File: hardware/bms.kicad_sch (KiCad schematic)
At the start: 15 parts

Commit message: train schematics
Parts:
- C? (x4): Voltage 10V -> 25V
- C?: value 22u -> 10u; Voltage 10V -> 25V
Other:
- note added: "0x40-0x4E/0x41-0x4F"
- note added: "0x6C/0x6D"
- company: Erdapfel -> Frisius
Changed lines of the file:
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@@
   (title_block
     (rev "A")
-    (company "Erdapfel")
+    (company "Frisius")
   )
   (junction (at 86.36 68.58) (diameter 0) (color 0 0 0 0)
@@
   (wire (pts (xy 46.99 66.04) (xy 46.99 67.31))
     (stroke (width 0) (type default) (color 0 0 0 0))
+  )
+  (text "0x40-0x4E/0x41-0x4F" (at 120.65 27.94 0)
+    (effects (font (size 1.27 1.27)) (justify left bottom))
+  )
+  (text "0x6C/0x6D" (at 120.65 59.69 0)
+    (effects (font (size 1.27 1.27)) (justify left bottom))
   )
   (label "USB_CHG.DP" (at 52.07 35.56 180)
@@
       (effects (font (size 0.8 0.8)) hide)
     )
-    (property "Voltage" "10V" (id 4) (at 88.9 74.93 0)
+    (property "Voltage" "25V" (id 4) (at 88.9 74.93 0)
       (effects (font (size 0.8 0.8)) (justify left))
     )
@@
       (effects (font (size 0.8 0.8)) hide)
     )
-    (property "Voltage" "10V" (id 4) (at 96.52 40.64 0)
+    (property "Voltage" "25V" (id 4) (at 96.52 40.64 0)
       (effects (font (size 0.8 0.8)) (justify left))
     )
@@
       (effects (font (size 0.8 0.8)) hide)
     )
-    (property "Voltage" "10V" (id 4) (at 96.52 58.42 0)
+    (property "Voltage" "25V" (id 4) (at 96.52 58.42 0)
       (effects (font (size 0.8 0.8)) (justify left))
     )
@@
       (effects (font (size 0.8 0.8)) (justify left))
     )
-    (property "Value" "22u" (id 1) (at 104.14 39.37 0)
+    (property "Value" "10u" (id 1) (at 104.14 39.37 0)
       (effects (font (size 0.8 0.8)) (justify left))
     )
@@
       (effects (font (size 0.8 0.8)) hide)
     )
-    (property "Voltage" "10V" (id 4) (at 104.14 40.64 0)
+    (property "Voltage" "25V" (id 4) (at 104.14 40.64 0)
       (effects (font (size 0.8 0.8)) (justify left))
     )
@@
       (effects (font (size 0.8 0.8)) hide)
     )
-    (property "Voltage" "10V" (id 4) (at 104.14 58.42 0)
-      (effects (font (size 0.8 0.8)) (justify left))
-    )
+    (property "Voltage" "25V" (id 4) (at 104.14 58.42 0)
+      (effects (font (size 0.8 0.8)) (justify left))
+    )

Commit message: usb, charger, sensors, heir
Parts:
- added C? (x2): 4.7u, Capacitor_SMD:C_0805_2012Metric, symbol Device:C_Small
- added D? (x2): LED_Small_Filled, symbol Device:LED_Small_Filled
- added R? (x2): 100k, Resistor_SMD:R_0603_1608Metric, symbol Device:R_Small
- added R? (x2): 1k, Resistor_SMD:R_0603_1608Metric, symbol Device:R_Small
- added R? (x3): 0, Resistor_SMD:R_0603_1608Metric, symbol Device:R_Small
- added R?: 100, Resistor_SMD:R_0603_1608Metric, symbol Device:R_Small
- added R? (x2): 14k, Resistor_SMD:R_0603_1608Metric, symbol Device:R_Small
- added R? (x2): 4.7k, Resistor_SMD:R_0603_1608Metric, symbol Device:R_Small
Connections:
- net GND: now also C?.2, C?.2, R?.2, R?.2
- net SENSOR_I2C.SCL: now also R?.2
- net SENSOR_I2C.SDA: now also R?.2
- net USB_SW: now also R?.2
- net +BATT: now reaches BT?.1 (+), C?.1, C?.1, U?.13_14 (BAT), U?.2 (CELL), U?.3 (VDD)
- net +BATT: now also C?.1, R?.2
- net at U?.11 (ITOPOFF): now also R?.1, R?.2
- net at U?.12 (IFAST): now also R?.1
- net at U?.2 (INOKB): now also R?.1, R?.1, R?.2
- net VBUS: now reaches U?.23_24 (CHGIN)
- net VBUS: now also C?.1, C?.1
- net at U?.3 (STAT): now also R?.1, R?.1, R?.2
- net at U?.8 (VCC): now also R?.1; no longer C?.1
- net THERM_SHDN renamed CHG_SHDN
- net CHG_SHDN: now also R?.1
- new net: D?.1 (K), R?.1 (x2)
- new net 3V3_CORE: D?.2 (A), D?.2 (A), R?.1, R?.1, R?.2, R?.2
- new net CHG_STAT: R?.2
- no-connect marks 0 -> 1
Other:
- note added: "DEBUG LEDS"
- note added: "Defaults: T_{th}=80C T_{hys}=75C OS Comparator OS Active Low"
- note added: "Hi-Z till LM75B thermal threshold which triggers thermal shutdown"
- note added: "I_{Fast}=2000mA I_{Topoff}=150mA"
- moved on the sheet: BT?, C?, L?, U?

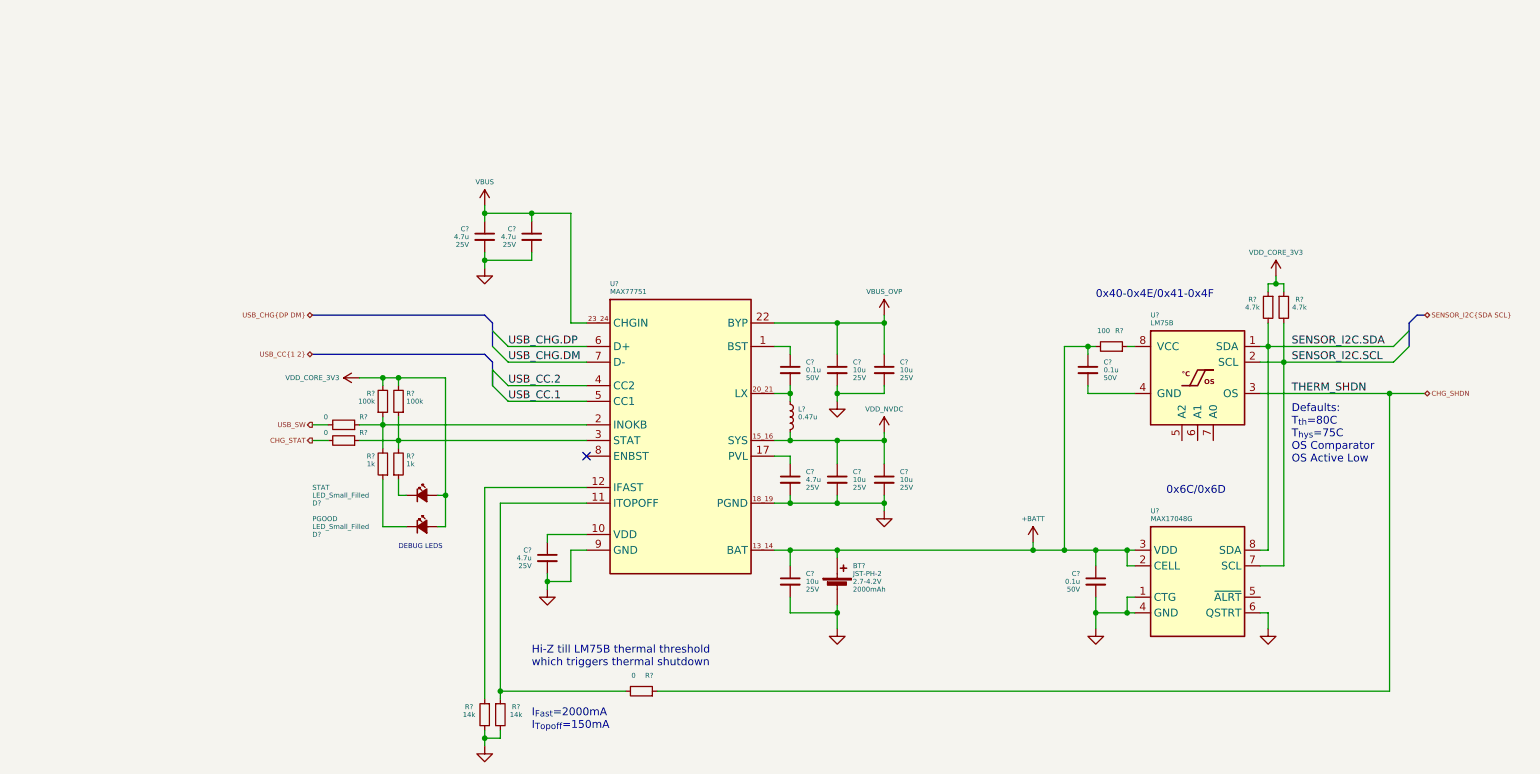
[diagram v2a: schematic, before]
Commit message: usb, bms, proc, btn changes
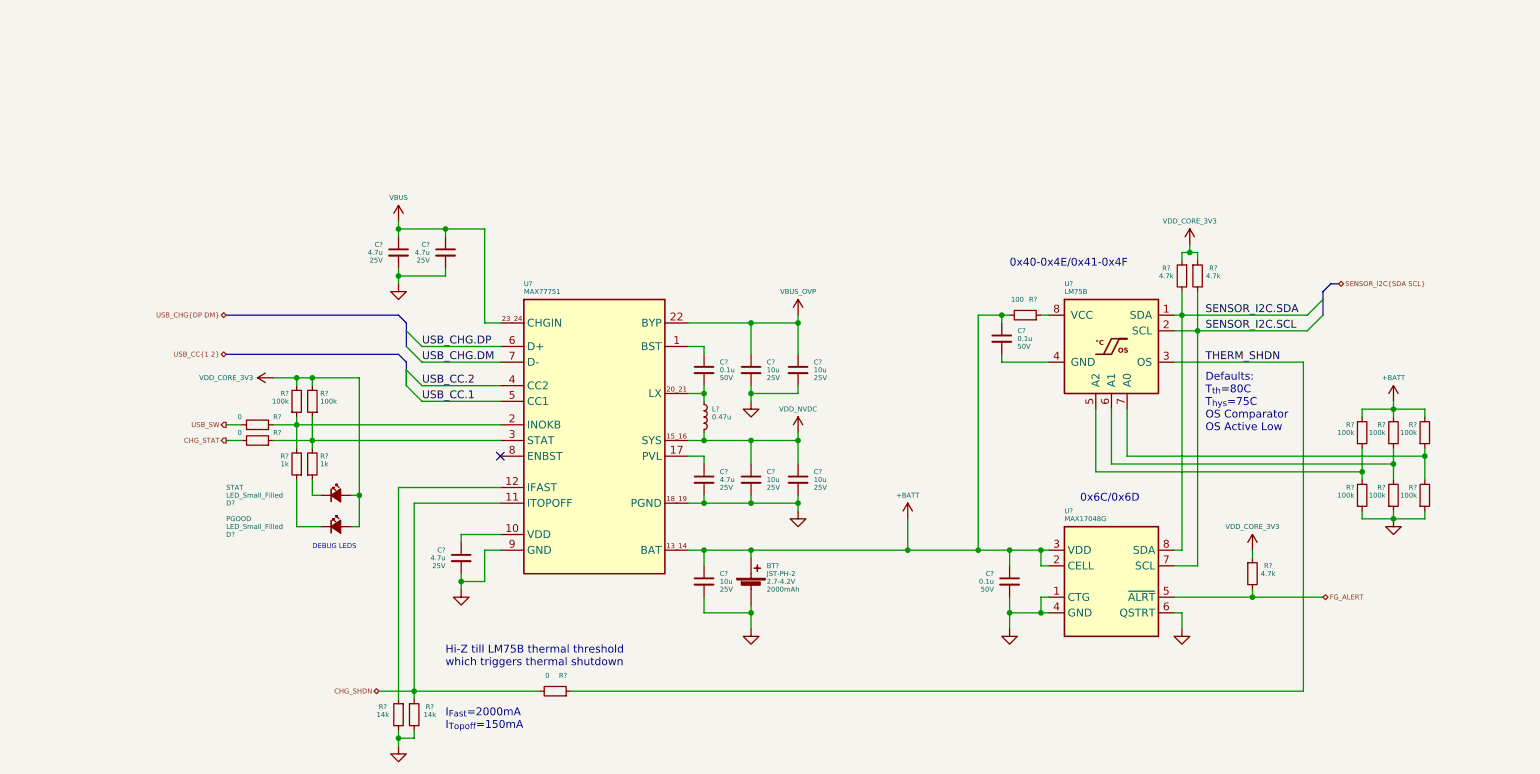
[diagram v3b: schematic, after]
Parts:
- added R? (x6): 100k, Resistor_SMD:R_0603_1608Metric, symbol Device:R_Small
- added R?: 4.7k, Resistor_SMD:R_0603_1608Metric, symbol Device:R_Small
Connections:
- net +BATT: now also R?.2, R?.2, R?.2
- net 3V3_CORE: now also R?.1
- net CHG_SHDN: now also R?.1, R?.2, U?.11 (ITOPOFF); no longer R?.1, U?.3 (OS)
- net GND: now also R?.1, R?.1, R?.1
- net at U?.5 (A2): now also R?.1, R?.2
- net at U?.6 (A1): now also R?.1, R?.2
- net at U?.7 (A0): now also R?.1, R?.2
- net FG_ALERT: now reaches U?.5 (~{ALRT})
- net FG_ALERT: now also R?.2
- new net THERM_SHDN: R?.1, U?.3 (OS)
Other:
- moved on the sheet: BT?, C?, D?, L?, R?, U?

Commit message: started b2b and power
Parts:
- added TP?: FG_ALERT, symbol Connector:TestPoint
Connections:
- net CHG_SHDN renamed CHARGE_SHDN
- net CHG_STAT renamed CHARGE_STAT
- net FG_ALERT: no longer names the net of R?.2, U?.5 (~{ALRT})
- net FG_ALERT: now also TP?.1
- net USB_SW renamed POWER_GOOD
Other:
- moved on the sheet: BT?, C?, D?, L?, R?, U?

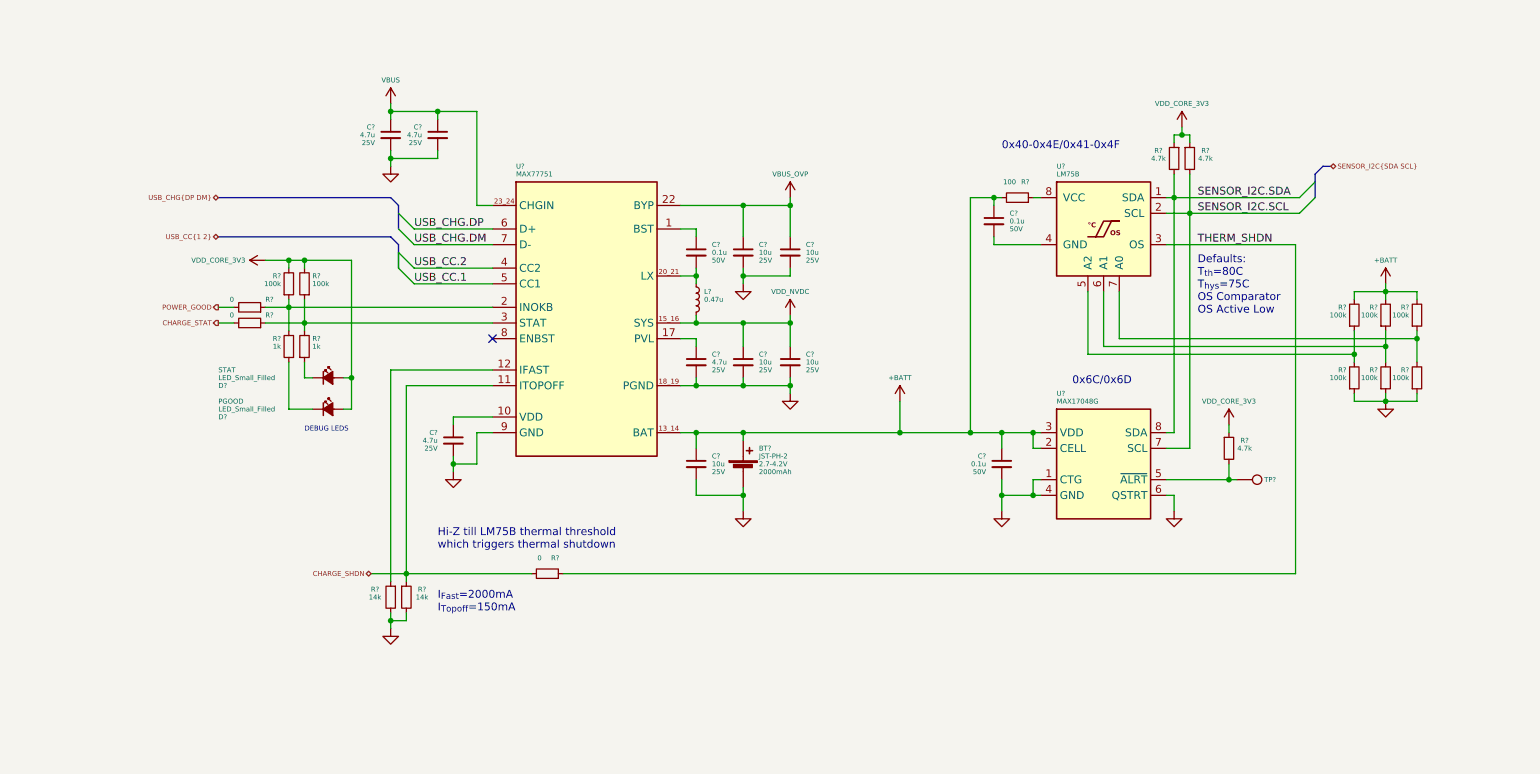
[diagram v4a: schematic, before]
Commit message: checking footprint assignment, added current sense pac1934 for dev
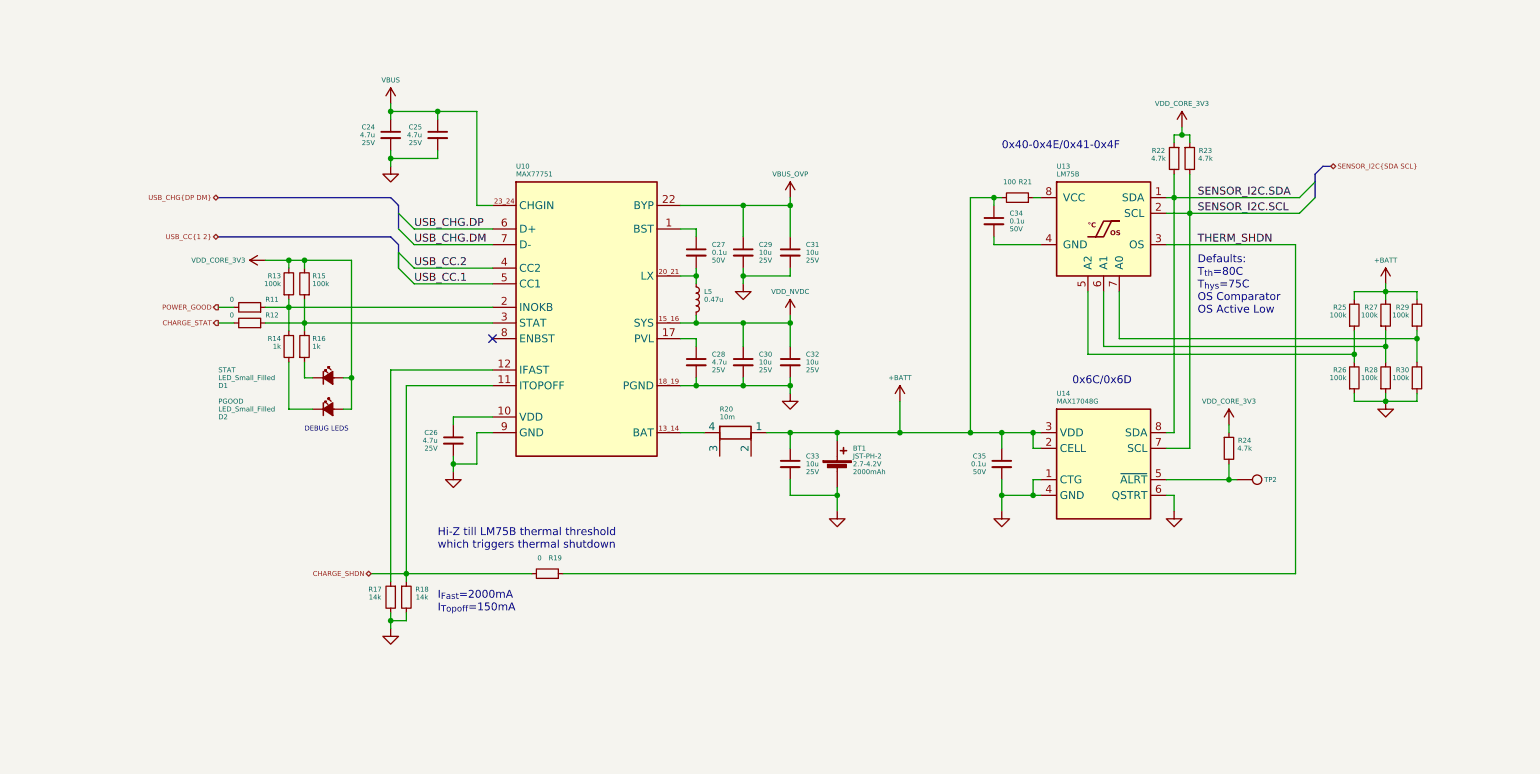
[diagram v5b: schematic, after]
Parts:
- added R20: 10m, Resistor_SMD:R_1210_3225Metric, symbol Device:R_Shunt
- BT1: renamed from BT?; footprint (none) -> Connector_JST:JST_PH_S2B-PH-SM4-TB_1x02-1MP_P2.00mm_Horizontal
- D1, D2: renamed from D?; footprint (none) -> LED_SMD:LED_0603_1608Metric
- L5: renamed from L?; footprint (none) -> Inductor_SMD:L_Bourns-SRN4018
- TP2: renamed from TP?; footprint (none) -> TestPoint:TestPoint_Pad_1.5x1.5mm
- U10: renamed from U?; footprint Package_QFN_bt:FC2QFN-24-3x3_P0.4mm -> bt_Package_QFN:FC2QFN-24-3x3_P0.4mm
- U13: renamed from U?; footprint (none) -> Package_DFN_QFN:DFN-8-1EP_2x2mm_P0.5mm_EP0.7x1.3mm
- gave numbers to parts that had none: 32
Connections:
- net +BATT: now also R20.1; no longer U10.13_14 (BAT)
- new net: R20.4, U10.13_14 (BAT)
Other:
- moved on the sheet: BT1, C33

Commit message: hardware update
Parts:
- removed C25: 4.7u, Capacitor_SMD:C_0805_2012Metric, symbol Device:C_Small
- removed R11, R12: 0, Resistor_SMD:R_0603_1608Metric, symbol Device:R_Small
- removed R15, R25, R26, R27, R28, R29, R30: 100k, Resistor_SMD:R_0603_1608Metric, symbol Device:R_Small
- removed R21: 100, Resistor_SMD:R_0603_1608Metric, symbol Device:R_Small
- removed TP2: FG_ALERT, TestPoint:TestPoint_Pad_1.5x1.5mm, symbol Connector:TestPoint
- BT1: footprint Connector_JST:JST_PH_S2B-PH-SM4-TB_1x02-1MP_P2.00mm_Horizontal -> Connector_PinHeader_1.00mm:PinHeader_1x02_P1.00mm_Vertical
- C20: renamed from C24; footprint Capacitor_SMD:C_0805_2012Metric -> Capacitor_SMD:C_0603_1608Metric
- C21: renamed from C26; footprint Capacitor_SMD:C_0805_2012Metric -> Capacitor_SMD:C_0603_1608Metric
- C22: renamed from C27; footprint Capacitor_SMD:C_0603_1608Metric -> Capacitor_SMD:C_0402_1005Metric
- C23: renamed from C28; footprint Capacitor_SMD:C_0805_2012Metric -> Capacitor_SMD:C_0603_1608Metric
- C29: renamed from C34; footprint Capacitor_SMD:C_0603_1608Metric -> Capacitor_SMD:C_0402_1005Metric
- C30: renamed from C35; footprint Capacitor_SMD:C_0603_1608Metric -> Capacitor_SMD:C_0402_1005Metric
- L3: renamed from L5; footprint Inductor_SMD:L_Bourns-SRN4018 -> Inductor_SMD:L_Wuerth_MAPI-2510
- R11: renamed from R13; footprint Resistor_SMD:R_0603_1608Metric -> Resistor_SMD:R_0402_1005Metric
- R12: renamed from R14; footprint Resistor_SMD:R_0603_1608Metric -> Resistor_SMD:R_0402_1005Metric
- R13: renamed from R16; footprint Resistor_SMD:R_0603_1608Metric -> Resistor_SMD:R_0402_1005Metric
- R14: renamed from R17; footprint Resistor_SMD:R_0603_1608Metric -> Resistor_SMD:R_0402_1005Metric
- R15: renamed from R18; footprint Resistor_SMD:R_0603_1608Metric -> Resistor_SMD:R_0402_1005Metric
- R16: renamed from R19; footprint Resistor_SMD:R_0603_1608Metric -> Resistor_SMD:R_0402_1005Metric
- R17: renamed from R20; footprint Resistor_SMD:R_1210_3225Metric -> Resistor_SMD:R_0603_1608Metric_Pad0.98x0.95mm_HandSolder
- R18: renamed from R22; footprint Resistor_SMD:R_0603_1608Metric -> Resistor_SMD:R_0402_1005Metric
- R19: renamed from R23; footprint Resistor_SMD:R_0603_1608Metric -> Resistor_SMD:R_0402_1005Metric
- R20: renamed from R24; footprint Resistor_SMD:R_0603_1608Metric -> Resistor_SMD:R_0402_1005Metric
- renumbered C29 to C24, C30 to C25, C31 to C26, C32 to C27, C33 to C28, D1 to D2, D2 to D3, U10 to U5, U13 to U6, U14 to U7
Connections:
- net +BATT: now also U6.8 (VCC)
- net GND: now also U6.5 (A2), U6.6 (A1), U6.7 (A0)
- net POWER_GOOD: now also R11.1, R12.2, U5.2 (INOKB)
- net I_{bat}.-: now reaches R17.2
- net I_{bat}.+: now reaches R17.3
- net CHARGE_SHDN: no longer names the net of R15.1, R16.2, U5.11 (ITOPOFF)
- net USB_CHG.DM renamed USB_CHG.D-
- net USB_CHG.DP renamed USB_CHG.D+
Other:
- moved on the sheet: C20
